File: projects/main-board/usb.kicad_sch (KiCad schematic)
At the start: 1 part

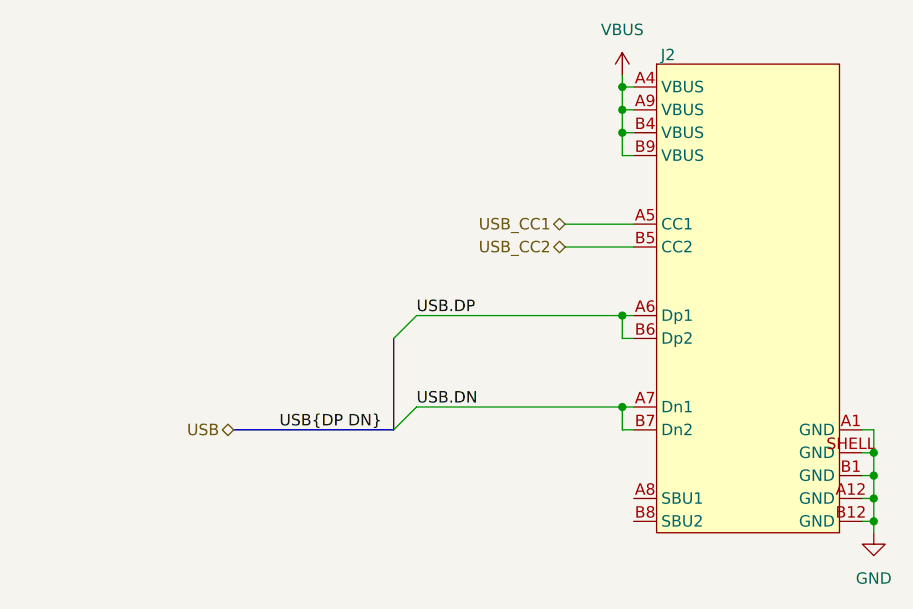
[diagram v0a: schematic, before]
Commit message: Updated schematics with new symbols
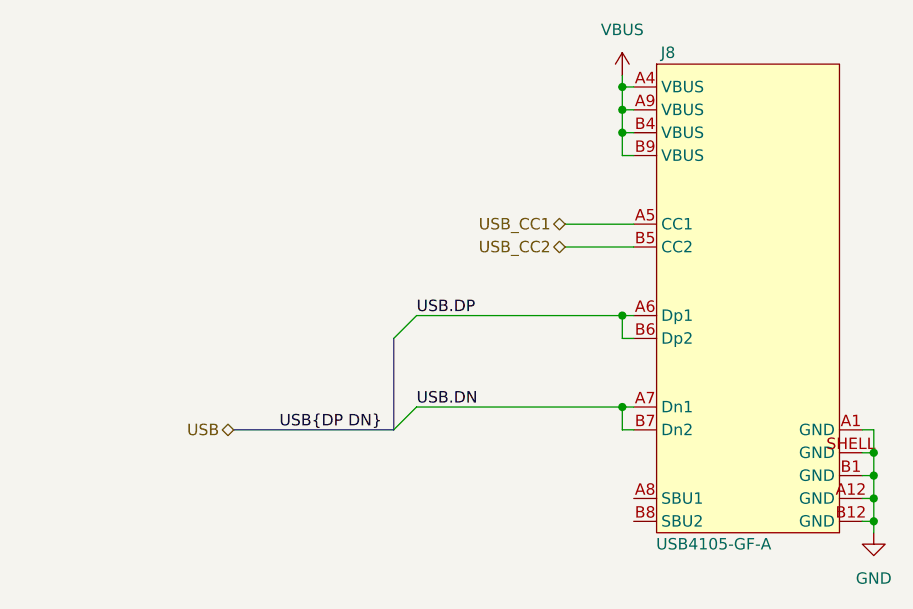
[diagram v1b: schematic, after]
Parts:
- removed J2: ~, symbol symbol-library:USB4105-GF-A
- added J8: USB4105-GF-A, footprint-library:USB4105-GF-A, symbol symbol-library:USB4105-GF-A
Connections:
- net GND: now also J8.A1 (GND), J8.A12 (GND), J8.B1 (GND), J8.B12 (GND), J8.SHELL (GND)
- net USB.DN: now also J8.A7 (Dn1), J8.B7 (Dn2)
- net USB.DP: now also J8.A6 (Dp1), J8.B6 (Dp2)
- net USB_CC1: now also J8.A5 (CC1)
- net USB_CC2: now also J8.B5 (CC2)
- net VBUS: now also J8.A4 (VBUS), J8.A9 (VBUS), J8.B4 (VBUS), J8.B9 (VBUS)
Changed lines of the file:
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@@
 	)
 	(symbol
+		(lib_name "USB4105-GF-A_1")
 		(lib_id "symbol-library:USB4105-GF-A")
 		(at 151.13 68.58 0)
@@
 		(on_board yes)
 		(dnp no)
-		(property "Reference" "J2"
-			(at 152.4 67.564 0)
+		(property "Reference" "J8"
+			(at 152.4 67.31 0)
 			(effects
 				(font
@@
 			)
 		)
-		(property "Value" "~"
-			(at 155.956 67.31 0)
+		(property "Value" "USB4105-GF-A"
+			(at 157.48 121.92 0)
 			(effects
 				(font
@@
 			)
 		)
-		(property "Footprint" ""
-			(at 151.13 68.58 0)
+		(property "Footprint" "footprint-library:USB4105-GF-A"
+			(at 163.83 123.698 0)
 			(effects
 				(font
@@
 		(pin "A4"
 		)
-		(pin "A9"
-		)
-		(pin "B4"
-		)
-		(pin "B9"
-		)
-		(pin "A5"
-		)
 		(pin "B5"
 		)
@@
 		(pin "B12"
 		)
+		(pin "B4"
+		)
+		(pin "B9"
+		)
+		(pin "A5"
+		)
+		(pin "A9"
+		)
 		(instances
 			(project ""
 				(path "/c621b5fd-2ef7-4a67-960d-0ffc72b1245a/d69ad104-b7d7-4317-8438-c35158ce58f7"
-					(reference "J2")
+					(reference "J8")
 					(unit 1)
 				)

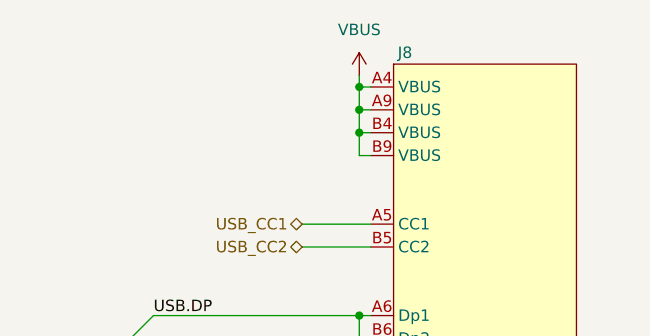
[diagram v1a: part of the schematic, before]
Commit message: Re-annotate schematics.
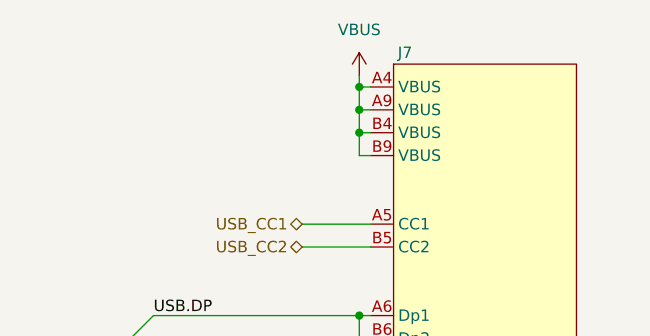
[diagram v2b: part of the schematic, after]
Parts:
- renumbered J8 to J7
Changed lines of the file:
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@@
 		(on_board yes)
 		(dnp no)
-		(property "Reference" "J8"
+		(property "Reference" "J7"
 			(at 152.4 67.31 0)
 			(effects
@@
 			(project ""
 				(path "/c621b5fd-2ef7-4a67-960d-0ffc72b1245a/d69ad104-b7d7-4317-8438-c35158ce58f7"
-					(reference "J8")
+					(reference "J7")
 					(unit 1)
 				)
@@
 		(dnp no)
 		(fields_autoplaced yes)
-		(property "Reference" "#PWR0131"
+		(property "Reference" "#PWR0148"
 			(at 175.26 127 0)
 			(effects
@@
 			(project ""
 				(path "/c621b5fd-2ef7-4a67-960d-0ffc72b1245a/d69ad104-b7d7-4317-8438-c35158ce58f7"
-					(reference "#PWR0131")
+					(reference "#PWR0148")
 					(unit 1)
 				)
@@
 		(dnp no)
 		(fields_autoplaced yes)
-		(property "Reference" "#PWR0129"
+		(property "Reference" "#PWR0147"
 			(at 147.32 73.66 0)
 			(effects
@@
 			(project ""
 				(path "/c621b5fd-2ef7-4a67-960d-0ffc72b1245a/d69ad104-b7d7-4317-8438-c35158ce58f7"
-					(reference "#PWR0129")
+					(reference "#PWR0147")
 					(unit 1)
 				)

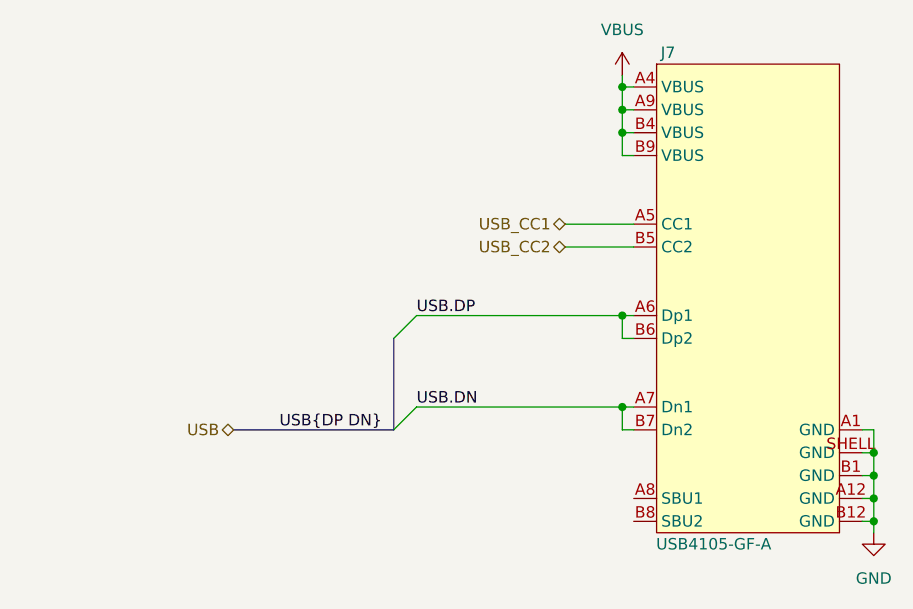
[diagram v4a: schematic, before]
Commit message: Fix footprint DRC errors.
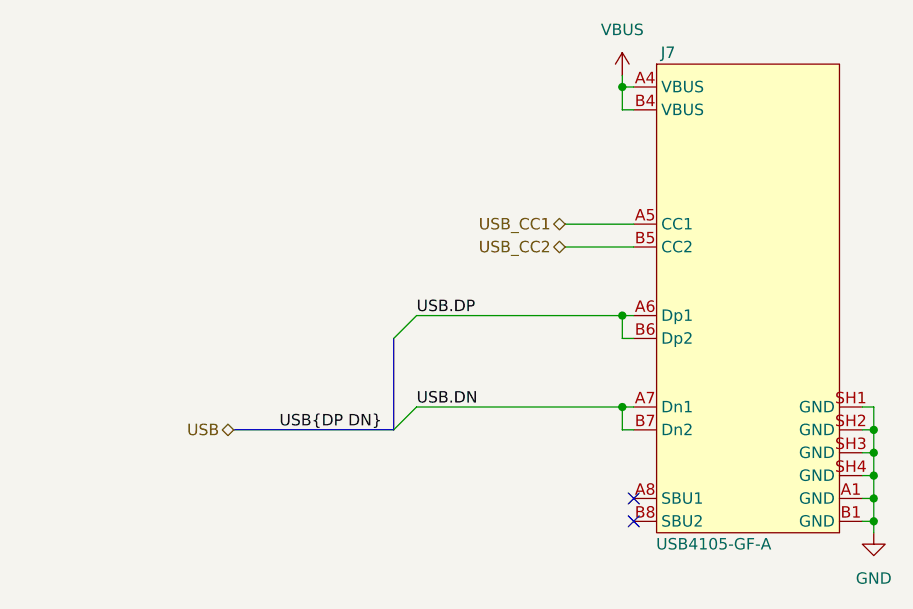
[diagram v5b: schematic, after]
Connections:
- net GND: now also J7.SH1 (GND), J7.SH2 (GND), J7.SH3 (GND), J7.SH4 (GND); no longer J7.A12 (GND), J7.B12 (GND), J7.SHELL (GND)
- net VBUS: no longer J7.A9 (VBUS), J7.B9 (VBUS)
- no-connect marks 0 -> 2
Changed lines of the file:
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@@
+	)
+	(junction
+		(at 175.26 109.22)
+		(diameter 0)
+		(color 0 0 0 0)
 	)
 	(junction
@@
 	)
 	(junction
-		(at 147.32 73.66)
-		(diameter 0)
-		(color 0 0 0 0)
-	)
-	(junction
 		(at 147.32 71.12)
-		(diameter 0)
-		(color 0 0 0 0)
-	)
-	(junction
-		(at 147.32 76.2)
 		(diameter 0)
 		(color 0 0 0 0)
@@
 		(color 0 0 0 0)
 	)
+	(no_connect
+		(at 148.59 119.38)
+	)
+	(no_connect
+		(at 148.59 116.84)
+	)
 	(bus_entry
 		(at 124.46 96.52)
@@
 	(wire
 		(pts
-			(xy 147.32 78.74) (xy 147.32 76.2)
-		)
-		(stroke
-			(width 0)
-			(type default)
-		)
-	)
-	(wire
-		(pts
 			(xy 124.46 106.68) (xy 147.32 106.68)
 		)
@@
 	(wire
 		(pts
+			(xy 173.99 106.68) (xy 175.26 106.68)
+		)
+		(stroke
+			(width 0)
+			(type default)
+		)
+	)
+	(wire
+		(pts
 			(xy 173.99 119.38) (xy 175.26 119.38)
 		)
@@
 	(wire
 		(pts
+			(xy 175.26 106.68) (xy 175.26 109.22)
+		)
+		(stroke
+			(width 0)
+			(type default)
+		)
+	)
+	(wire
+		(pts
 			(xy 124.46 96.52) (xy 147.32 96.52)
 		)
@@
 	(wire
 		(pts
-			(xy 148.59 78.74) (xy 147.32 78.74)
-		)
-		(stroke
-			(width 0)
-			(type default)
-		)
-	)
-	(wire
-		(pts
 			(xy 175.26 109.22) (xy 173.99 109.22)
 		)
@@
 		(pts
 			(xy 147.32 106.68) (xy 148.59 106.68)
-		)
-		(stroke
-			(width 0)
-			(type default)
-		)
-	)
-	(wire
-		(pts
-			(xy 147.32 76.2) (xy 148.59 76.2)
-		)
-		(stroke
-			(width 0)
-			(type default)
-		)
-	)
-	(wire
-		(pts
-			(xy 147.32 76.2) (xy 147.32 73.66)
 		)
 		(stroke
@@
 	)
 	(symbol
-		(lib_name "USB4105-GF-A_1")
 		(lib_id "symbol-library:USB4105-GF-A")
 		(at 151.13 68.58 0)
@@
 		(pin "A1"
 		)
-		(pin "SHELL"
+		(pin "SH1"
 		)
 		(pin "B1"
 		)
-		(pin "A12"
-		)
-		(pin "B12"
-		)
 		(pin "B4"
 		)
-		(pin "B9"
-		)
 		(pin "A5"
 		)
-		(pin "A9"
+		(pin "SH2"
+		)
+		(pin "SH3"
+		)
+		(pin "SH4"
 		)
 		(instances

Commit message: WIP splitting main board into 3
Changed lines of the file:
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@@
 		(at 148.59 116.84)
 	)
-	(bus_entry
-		(at 124.46 96.52)
-		(size -2.54 2.54)
-		(stroke
-			(width 0)
-			(type default)
-		)
-	)
-	(bus_entry
-		(at 124.46 106.68)
-		(size -2.54 2.54)
-		(stroke
-			(width 0)
-			(type default)
-		)
-	)
 	(wire
 		(pts
@@
 	(wire
 		(pts
-			(xy 124.46 106.68) (xy 147.32 106.68)
+			(xy 132.08 106.68) (xy 147.32 106.68)
 		)
 		(stroke
@@
 	(bus
 		(pts
-			(xy 104.14 109.22) (xy 121.92 109.22)
+			(xy 91.44 69.85) (xy 109.22 69.85)
 		)
 		(stroke
@@
 		)
 	)
-	(bus
-		(pts
-			(xy 121.92 99.06) (xy 121.92 109.22)
-		)
-		(stroke
-			(width 0)
-			(type default)
-		)
-	)
 	(wire
 		(pts
@@
 	(wire
 		(pts
-			(xy 140.97 88.9) (xy 148.59 88.9)
+			(xy 132.08 88.9) (xy 148.59 88.9)
 		)
 		(stroke
@@
 	(wire
 		(pts
-			(xy 124.46 96.52) (xy 147.32 96.52)
+			(xy 132.08 96.52) (xy 147.32 96.52)
 		)
 		(stroke
@@
 	(wire
 		(pts
+			(xy 91.44 76.2) (xy 109.22 76.2)
+		)
+		(stroke
+			(width 0)
+			(type default)
+		)
+	)
+	(wire
+		(pts
+			(xy 91.44 73.66) (xy 109.22 73.66)
+		)
+		(stroke
+			(width 0)
+			(type default)
+		)
+	)
+	(wire
+		(pts
 			(xy 173.99 111.76) (xy 175.26 111.76)
 		)
@@
 	(wire
 		(pts
-			(xy 140.97 86.36) (xy 148.59 86.36)
+			(xy 132.08 86.36) (xy 148.59 86.36)
 		)
 		(stroke
@@
 	)
 	(label "USB.DP"
-		(at 124.46 96.52 0)
+		(at 132.08 96.52 0)
+		(effects
+			(font
+				(size 1.27 1.27)
+			)
+			(justify left bottom)
+		)
+	)
+	(label "USB_CC1"
+		(at 96.52 73.66 0)
+		(effects
+			(font
+				(size 1.27 1.27)
+			)
+			(justify left bottom)
+		)
+	)
+	(label "USB_CC2"
+		(at 132.08 88.9 0)
+		(effects
+			(font
+				(size 1.27 1.27)
+			)
+			(justify left bottom)
+		)
+	)
+	(label "USB_CC2"
+		(at 96.52 76.2 0)
 		(effects
 			(font
@@
 	)
 	(label "USB.DN"
-		(at 124.46 106.68 0)
+		(at 132.08 106.68 0)
 		(effects
 			(font
@@
 	)
 	(label "USB{DP DN}"
-		(at 109.22 109.22 0)
-		(effects
-			(font
-				(size 1.27 1.27)
-			)
-			(justify left bottom)
+		(at 96.52 69.85 0)
+		(effects
+			(font
+				(size 1.27 1.27)
+			)
+			(justify left bottom)
+		)
+	)
+	(label "USB_CC1"
+		(at 132.08 86.36 0)
+		(effects
+			(font
+				(size 1.27 1.27)
+			)
+			(justify left bottom)
+		)
+	)
+	(hierarchical_label "USB"
+		(shape bidirectional)
+		(at 91.44 69.85 180)
+		(effects
+			(font
+				(size 1.27 1.27)
+			)
+			(justify right)
+		)
+	)
+	(hierarchical_label "USB_CC2"
+		(shape bidirectional)
+		(at 91.44 76.2 180)
+		(effects
+			(font
+				(size 1.27 1.27)
+			)
+			(justify right)
 		)
 	)
 	(hierarchical_label "USB_CC1"
 		(shape bidirectional)
-		(at 140.97 86.36 180)
-		(effects
-			(font
-				(size 1.27 1.27)
-			)
-			(justify right)
-		)
-	)
-	(hierarchical_label "USB"
-		(shape bidirectional)
-		(at 104.14 109.22 180)
-		(effects
-			(font
-				(size 1.27 1.27)
-			)
-			(justify right)
-		)
-	)
-	(hierarchical_label "USB_CC2"
-		(shape bidirectional)
-		(at 140.97 88.9 180)
-		(effects
-			(font
+		(at 91.44 73.66 180)
+		(effects
+			(font
